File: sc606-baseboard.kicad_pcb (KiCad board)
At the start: 6 copper layers, 100 x 90 mm, 425 parts, among them IC1 TPS54561DPRT, IC2 TPS7A0518PDBVT, J1 PJ-202A, J10 WE_632723300011, J11 WE_632723300011, J12 U_FL-R-SMT-1_10_, J13 WE_632723300011, J14 CONMMCX002-SMD-T, J2 WE_68715014522, J3 F52R-1A7H1-11020, J4 46756-1001, J5 U_FL-R-SMT-1_10_, J6 U_FL-R-SMT-1_10_, J7 DM3AT-SF-PEJM5, J8 693022010811, J9 0473460001, M1 SC606T, Q1 BSS138APW, Q2 BSS138-7-F, Q3 BSS138APW, Q4 BSS138APW, Q5 BSS138APW, Q6 BSS138APW, Q7 BSS138-7-F, Q8 BSS138-7-F, SW1 1X03, U1 AP62301WU-7, U10 NCP163ASN330T1G, U11 EMIF06-MSD02N16, U12 FSUSB30MUX, U13 FT232RQ-REEL, U15 USB57442G, U2 AP62301WU-7, U3 AP62301WU-7, U4 74LVC1G123GN, U5 NTS0102GT, U6 PCA9547BS, U7 LT9611UXC, U8 NTS0102GT, U9 TPD13S523PWR, Y1 ABM8G-24.000MHZ-18-D2Y-T, Y2 ABM8G-25.000MHZ-B4Y-T

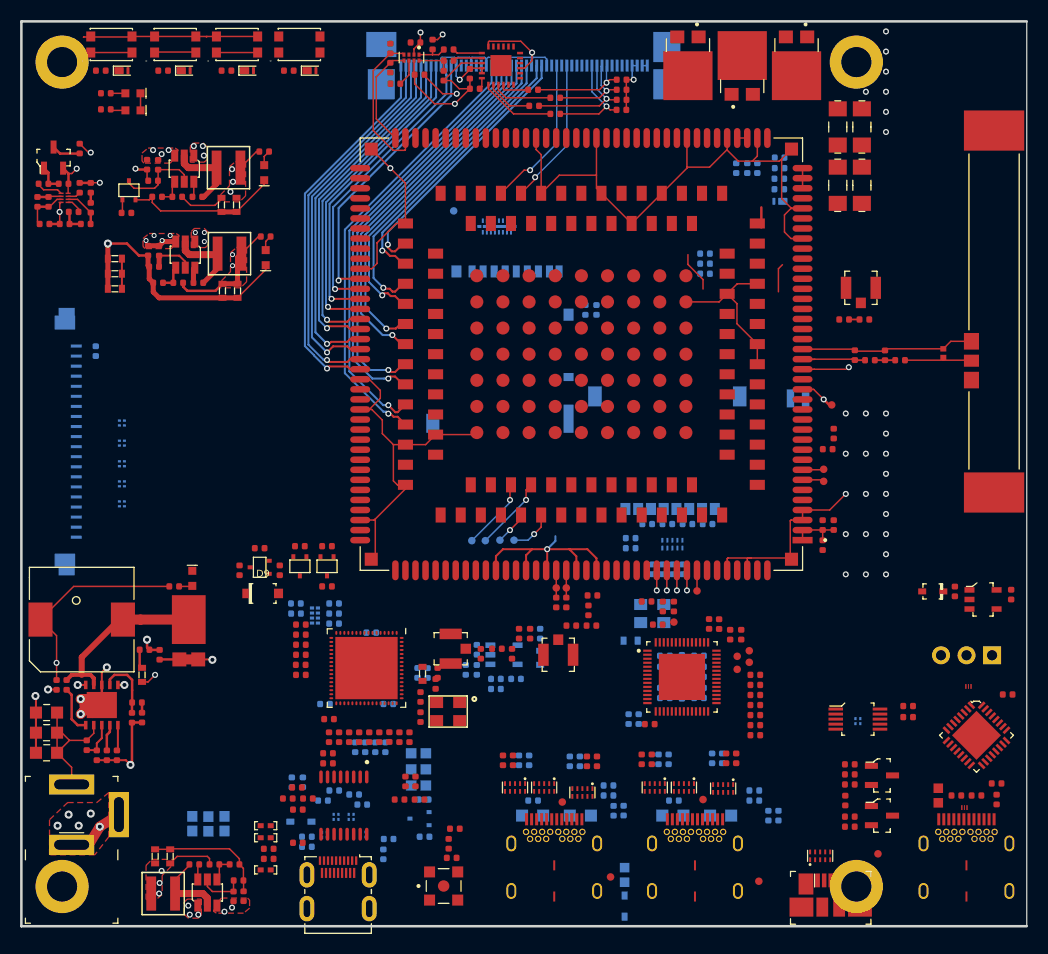
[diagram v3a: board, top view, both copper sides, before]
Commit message: USB Debug changed to micro USB. Started modifications on shortening board by 1cm
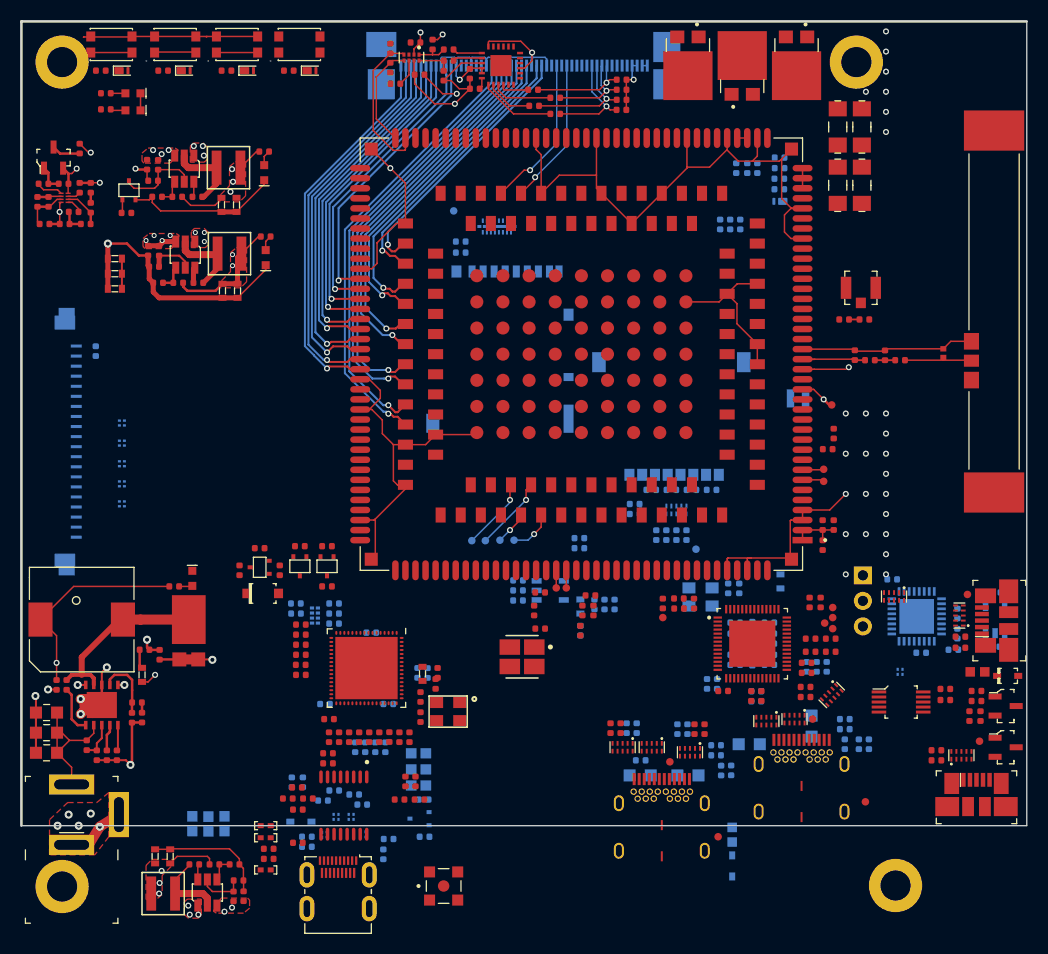
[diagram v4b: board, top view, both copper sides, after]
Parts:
- removed J10: WE_632723300011, sc606-baseboard-footprints:WE_632723300011
- removed J12: U_FL-R-SMT-1_10_, sc606-baseboard-footprints:Coax_Conn_U.FL
- removed R138, R139, R140: R_0R_0402, sc606-baseboard-footprints:0402-res
- added ANT1: 47948-0001, antmicro-footprints:47948-0001, F.Cu at (124.8, 103.2)
- added TP20: TP_SMD_0_75MM, sc606-baseboard-footprints:Testpoint_smd_0_75mm, F.Cu at (169.1, 97.1)
- C111, C112, C113, C114, C115, C116, C117, C118, C119, C126, C130, C132, IC2, R2, R3, TP2, U13: moved to B.Cu
- C142: value C_1u_0402 -> C_100n_0402
- C143: value C_1u_0402 -> C_4u7_0402
- D21, D23: value PESD5V0C2BDFZ -> PUSB3F96X_PASS; footprint sc606-baseboard-footprints:DFN0603-3 -> sc606-baseboard-footprints:PUSB3F96X
- J6: value U_FL-R-SMT-1_10_ -> 0473460001; footprint sc606-baseboard-footprints:Coax_Conn_U.FL -> sc606-baseboard-footprints:USB_Micro_B_Female_0473460001
- R134, R135: moved to F.Cu
- moved C143 54.7 mm to (168.4, 102.3), turned to 180 degrees
- moved C142 53.8 mm to (168.4, 101.2), turned to 180 degrees
- moved J6 44.9 mm to (173.2, 99.6), turned to 270 degrees
- moved D21 19.1 mm to (168.3, 99.1), turned to 90 degrees
- moved C112 18.1 mm to (168.1, 98.9), turned to 90 degrees
- moved C151 17.9 mm to (156.9, 111.9), turned to 90 degrees
- moved J9 17.6 mm to (170.0, 118.1)
- moved D20 17.2 mm to (168.5, 113.0)
- moved C113 16.2 mm to (161.6, 95.5), turned to 180 degrees
- moved C114 16.2 mm to (168.1, 100.9), turned to 270 degrees
- moved R113 16.0 mm to (150.5, 95.7), turned to 270 degrees
- moved C117 15.5 mm to (167.7, 102.5), turned to 180 degrees
- moved SW1 15.1 mm to (158.7, 95.1), turned to 0 degrees
- moved TP12 15.1 mm to (170.3, 111.7)
- moved C116 15.0 mm to (164.5, 102.8)
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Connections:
- C142 pad 1: Net-(C142-Pad1) -> /USB_flash_debug/DBG_VBUS
- C143 pad 1: Net-(C143-Pad1) -> /USB_flash_debug/DBG_VBUS
- C89 pad 1: Net-(C89-Pad1) -> ANT-WIFI
- D23 pad 1: DEBUG_UART_RX -> Net-(D23-Pad1)
- D23 pad 2: DEBUG_UART_TX -> Net-(D23-Pad2)
- D32 pad 1: /USB_HUB_Connectors/USB_C2_SS_C_TX2_N -> /USB_HUB_Connectors/USB_C2_SS_C_RX2_P
- D32 pad 10: /USB_HUB_Connectors/USB_C2_SS_C_TX2_N -> /USB_HUB_Connectors/USB_C2_SS_C_RX2_P
- D32 pad 2: /USB_HUB_Connectors/USB_C2_SS_C_TX2_P -> /USB_HUB_Connectors/USB_C2_SS_C_RX2_N
- D32 pad 4: /USB_HUB_Connectors/USB_C2_SS_C_RX2_P -> /USB_HUB_Connectors/USB_C2_SS_C_TX2_N
- D32 pad 5: /USB_HUB_Connectors/USB_C2_SS_C_RX2_N -> /USB_HUB_Connectors/USB_C2_SS_C_TX2_P
- D32 pad 6: /USB_HUB_Connectors/USB_C2_SS_C_RX2_N -> /USB_HUB_Connectors/USB_C2_SS_C_TX2_P
- D32 pad 7: /USB_HUB_Connectors/USB_C2_SS_C_RX2_P -> /USB_HUB_Connectors/USB_C2_SS_C_TX2_N
- D32 pad 9: /USB_HUB_Connectors/USB_C2_SS_C_TX2_P -> /USB_HUB_Connectors/USB_C2_SS_C_RX2_N
- J14 pad 1: Net-(C143-Pad1) -> Net-(C101-Pad1)
- J6 pad 1: GND -> /USB_flash_debug/DBG_VBUS
- J6 pad 2: Net-(C101-Pad1) -> /USB_flash_debug/DBG_USB_D_N
- R126 pad 1: Net-(C89-Pad1) -> ANT-WIFI
- SW1 pad 1: DEBUG_UART_RX -> DEBUG_UART_TX
- SW1 pad 2: DEBUG_UART_TX -> DEBUG_UART_RX
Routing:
- net GND: track 350.0 -> 328.2 mm, vias 56 -> 54
- net SD_DATA_6: track 4.05 -> 0.00 mm
- net SD_LDO11: track 2.87 -> 0.00 mm
- net (no net): track 2.40 -> 0.00 mm
- net USIM1_VDD: track 2.14 -> 0.00 mm, vias 1 -> 0
- net Net-(M1-Pad145): track 2.05 -> 0.00 mm
- net USIM1_RST: track 2.00 -> 0.00 mm, vias 1 -> 0
- net USIM1_DATA: track 2.00 -> 0.00 mm, vias 1 -> 0
- net USIM1_CLK: track 2.00 -> 0.00 mm, vias 1 -> 0
- net Net-(M1-Pad132): track 2.72 -> 1.75 mm
- net Net-(M1-Pad131): track 2.72 -> 1.75 mm
- net DEBUG_UART_TX: vias 0 -> 1
- added copper zone on In1.Power_Plane, net GND
- removed copper zone on In1.GND, net GND
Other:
- board size 100 x 90 mm -> 100 x 80 mm
- net class CSI_DSI_Inner removed
- net class CSI_DSI_Outer removed
- net class Default: clearance 0.15 -> 0.125; trace_width 0.15 -> 0.125
- net class HDMI_Inner removed
- net class SE50_inner added: clearance 0.125, trace_width 0.162, via_dia 0.6, via_drill 0.35
- net class SE50_outer added: clearance 0.125, trace_width 0.182, via_dia 0.6, via_drill 0.35
- net class Z100_inner added: clearance 0.125, trace_width 0.162, via_dia 0.6, via_drill 0.35
- net class Z100_outer added: clearance 0.125, trace_width 0.182, via_dia 0.6, via_drill 0.35
- net class Z90_inner added: clearance 0.125, trace_width 0.193, via_dia 0.6, via_drill 0.35
- net class Z90_outer added: clearance 0.125, trace_width 0.215, via_dia 0.6, via_drill 0.35
- rule trace_clearance: 0.15 -> 0.125
- rule trace_min: 0.15 -> 0.125

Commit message: Finished placement after shortening board by 1cm
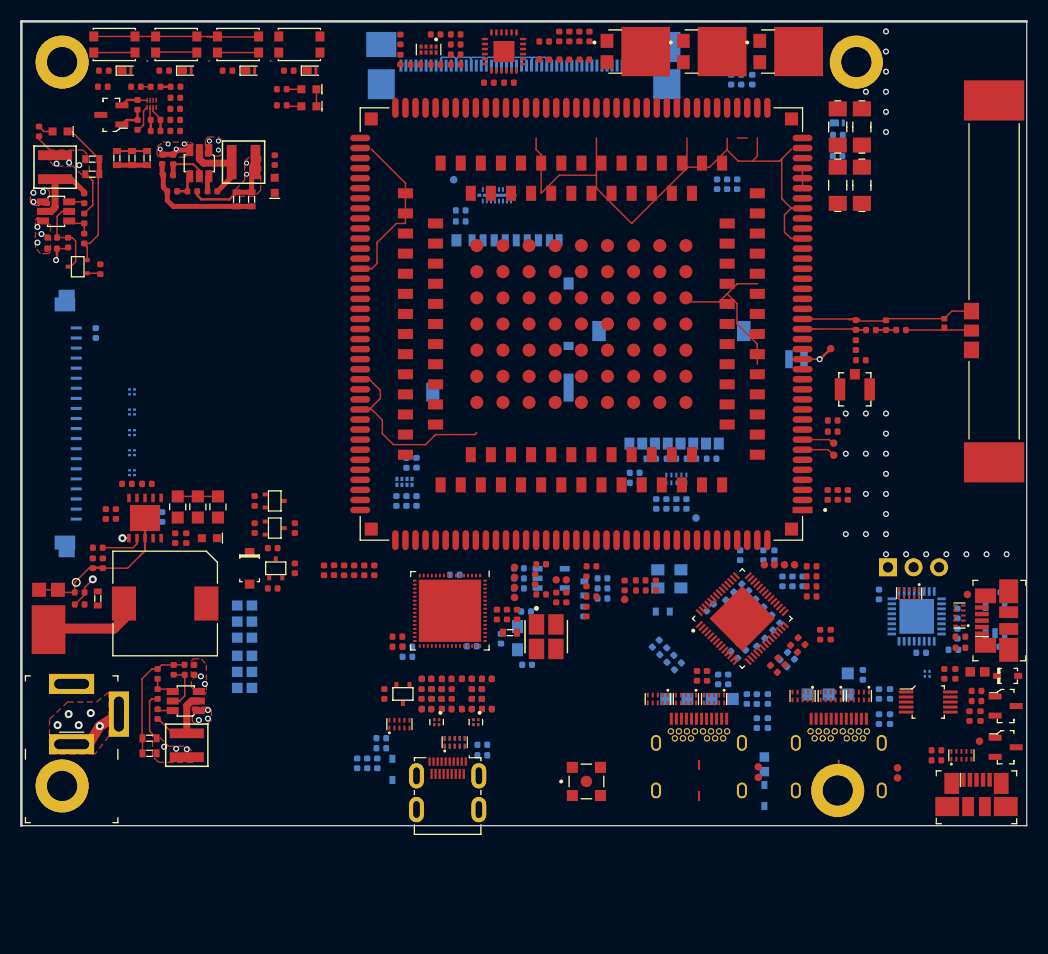
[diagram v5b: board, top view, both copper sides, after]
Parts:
- removed C83, C84: C_100n_0402, sc606-baseboard-footprints:0402-cap
- removed D7, D8: TPD1E10B06DPYR, sc606-baseboard-footprints:XDFN-2_1x0.60mm
- removed R155, R156, R157, R158: R_0R_0402, sc606-baseboard-footprints:0402-res
- removed U9: TPD13S523PWR, sc606-baseboard-footprints:TSSOP-16
- added D29: PUSB3F96X_PASS, sc606-baseboard-footprints:PUSB3F96X, F.Cu at (118.1, 111.7)
- added D30: PUSB3F96X_PASS, sc606-baseboard-footprints:PUSB3F96X, B.Cu at (118.1, 111.7)
- added R138: R_56k_0402, antmicro-footprints:0402-res, B.Cu at (161.4, 106.9)
- added R139: R_56k_0402, antmicro-footprints:0402-res, B.Cu at (161.4, 109.4)
- added R140: R_56k_0402, antmicro-footprints:0402-res, B.Cu at (160.3, 106.9)
- added R141: R_56k_0402, antmicro-footprints:0402-res, B.Cu at (160.3, 109.4)
- C128, C25, C53, C57, R118, R119, R130, R133, R136, R137, R52, R61, R62, R65, R66, R67, R68, R88, Y1: moved to B.Cu
- C147, C149, C67, C68, C77, C78, C80, L16, L18, Q3, R2, R3, TP5, TP6, TP7, TP8: moved to F.Cu
- D6: value TPD1E10B06DPYR -> PUSB3F96X_PASS; footprint sc606-baseboard-footprints:XDFN-2_1x0.60mm -> sc606-baseboard-footprints:PUSB3F96X
- R123, R125, R131, R132: value R_0R_0402 -> R_56k_0402; footprint sc606-baseboard-footprints:0402-res -> antmicro-footprints:0402-res
- moved C19 29.8 mm to (94.5, 88.3), turned to 270 degrees
- moved R5 27.2 mm to (85.5, 86.0), turned to 180 degrees
- moved C17 27.0 mm to (92.5, 88.3), turned to 270 degrees
- moved R4 26.7 mm to (87.5, 86.0), turned to 180 degrees
- moved C18 24.3 mm to (90.5, 88.3), turned to 270 degrees
- moved C20 24.0 mm to (83.4, 89.0)
- moved R6 24.0 mm to (84.4, 89.0)
- moved C21 23.6 mm to (91.7, 104.0), turned to 180 degrees
- moved L5 22.7 mm to (97.2, 98.1)
- moved L6 22.7 mm to (97.2, 99.7)
- moved L7 22.7 mm to (97.2, 101.3)
- moved R106 22.5 mm to (76.8, 51.0), turned to 90 degrees
- moved R7 22.5 mm to (91.7, 105.0), turned to 180 degrees
- moved R8 21.9 mm to (90.2, 104.5), turned to 90 degrees
- moved D19 20.7 mm to (78.8, 51.0), turned to 180 degrees
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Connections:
- D10 pad A: Net-(C84-Pad1) -> 5V0_SYS
- D25 pad 1: /USB_HUB_Connectors/USB_C1_D1_N -> /USB_HUB_Connectors/USB_C1_D2_N
- D25 pad 10: /USB_HUB_Connectors/USB_C1_D1_N -> /USB_HUB_Connectors/USB_C1_D2_N
- D25 pad 2: /USB_HUB_Connectors/USB_C1_D1_P -> /USB_HUB_Connectors/USB_C1_D2_P
- D25 pad 4: /USB_HUB_Connectors/USB_C1_D2_N -> /USB_HUB_Connectors/USB_C1_D1_N
- D25 pad 5: /USB_HUB_Connectors/USB_C1_D2_P -> /USB_HUB_Connectors/USB_C1_D1_P
- D25 pad 6: /USB_HUB_Connectors/USB_C1_D2_P -> /USB_HUB_Connectors/USB_C1_D1_P
- D25 pad 7: /USB_HUB_Connectors/USB_C1_D2_N -> /USB_HUB_Connectors/USB_C1_D1_N
- D25 pad 9: /USB_HUB_Connectors/USB_C1_D1_P -> /USB_HUB_Connectors/USB_C1_D2_P
- D26 pad 1: /USB_HUB_Connectors/USB_C2_SS_C_TX1_N -> /USB_HUB_Connectors/USB_C2_SS_C_RX1_N
- D26 pad 10: /USB_HUB_Connectors/USB_C2_SS_C_TX1_N -> /USB_HUB_Connectors/USB_C2_SS_C_RX1_N
- D26 pad 2: /USB_HUB_Connectors/USB_C2_SS_C_TX1_P -> /USB_HUB_Connectors/USB_C2_SS_C_RX1_P
- D26 pad 4: /USB_HUB_Connectors/USB_C2_SS_C_RX1_N -> /USB_HUB_Connectors/USB_C2_SS_C_TX1_N
- D26 pad 5: /USB_HUB_Connectors/USB_C2_SS_C_RX1_P -> /USB_HUB_Connectors/USB_C2_SS_C_TX1_P
- D26 pad 6: /USB_HUB_Connectors/USB_C2_SS_C_RX1_P -> /USB_HUB_Connectors/USB_C2_SS_C_TX1_P
- D26 pad 7: /USB_HUB_Connectors/USB_C2_SS_C_RX1_N -> /USB_HUB_Connectors/USB_C2_SS_C_TX1_N
- D26 pad 9: /USB_HUB_Connectors/USB_C2_SS_C_TX1_P -> /USB_HUB_Connectors/USB_C2_SS_C_RX1_P
- D27 pad 1: /USB_HUB_Connectors/USB_C1_SS_C_TX2_N -> /USB_HUB_Connectors/USB_C1_SS_C_RX2_P
- D27 pad 10: /USB_HUB_Connectors/USB_C1_SS_C_TX2_N -> /USB_HUB_Connectors/USB_C1_SS_C_RX2_P
- D27 pad 2: /USB_HUB_Connectors/USB_C1_SS_C_TX2_P -> /USB_HUB_Connectors/USB_C1_SS_C_RX2_N
- D27 pad 4: /USB_HUB_Connectors/USB_C1_SS_C_RX2_P -> /USB_HUB_Connectors/USB_C1_SS_C_TX2_N
- D27 pad 5: /USB_HUB_Connectors/USB_C1_SS_C_RX2_N -> /USB_HUB_Connectors/USB_C1_SS_C_TX2_P
- D27 pad 6: /USB_HUB_Connectors/USB_C1_SS_C_RX2_N -> /USB_HUB_Connectors/USB_C1_SS_C_TX2_P
- D27 pad 7: /USB_HUB_Connectors/USB_C1_SS_C_RX2_P -> /USB_HUB_Connectors/USB_C1_SS_C_TX2_N
- D27 pad 9: /USB_HUB_Connectors/USB_C1_SS_C_TX2_P -> /USB_HUB_Connectors/USB_C1_SS_C_RX2_N
- D28 pad 1: /USB_HUB_Connectors/USB_C1_SS_C_TX1_N -> /USB_HUB_Connectors/USB_C1_SS_C_RX1_N
- D28 pad 10: /USB_HUB_Connectors/USB_C1_SS_C_TX1_N -> /USB_HUB_Connectors/USB_C1_SS_C_RX1_N
- D28 pad 2: /USB_HUB_Connectors/USB_C1_SS_C_TX1_P -> /USB_HUB_Connectors/USB_C1_SS_C_RX1_P
- D28 pad 4: /USB_HUB_Connectors/USB_C1_SS_C_RX1_N -> /USB_HUB_Connectors/USB_C1_SS_C_TX1_N
- D28 pad 5: /USB_HUB_Connectors/USB_C1_SS_C_RX1_P -> /USB_HUB_Connectors/USB_C1_SS_C_TX1_P
- D28 pad 6: /USB_HUB_Connectors/USB_C1_SS_C_RX1_P -> /USB_HUB_Connectors/USB_C1_SS_C_TX1_P
- D28 pad 7: /USB_HUB_Connectors/USB_C1_SS_C_RX1_N -> /USB_HUB_Connectors/USB_C1_SS_C_TX1_N
- D28 pad 9: /USB_HUB_Connectors/USB_C1_SS_C_TX1_P -> /USB_HUB_Connectors/USB_C1_SS_C_RX1_P
- D31 pad 1: /USB_HUB_Connectors/USB_C2_D1_N -> /USB_HUB_Connectors/USB_C2_D2_P
- D31 pad 10: /USB_HUB_Connectors/USB_C2_D1_N -> /USB_HUB_Connectors/USB_C2_D2_P
- D31 pad 2: /USB_HUB_Connectors/USB_C2_D1_P -> /USB_HUB_Connectors/USB_C2_D2_N
- D31 pad 4: /USB_HUB_Connectors/USB_C2_D2_N -> /USB_HUB_Connectors/USB_C2_D1_N
- D31 pad 5: /USB_HUB_Connectors/USB_C2_D2_P -> /USB_HUB_Connectors/USB_C2_D1_P
- D31 pad 6: /USB_HUB_Connectors/USB_C2_D2_P -> /USB_HUB_Connectors/USB_C2_D1_P
- D31 pad 7: /USB_HUB_Connectors/USB_C2_D2_N -> /USB_HUB_Connectors/USB_C2_D1_N
- D31 pad 9: /USB_HUB_Connectors/USB_C2_D1_P -> /USB_HUB_Connectors/USB_C2_D2_N
- D6 pad 1: GND -> Net-(D6-Pad1)
- D6 pad 2: /display module/LTtoHDMI_SCL -> /display module/LTtoHDMI_SDA
- J11 pad A5: Net-(J11-PadA5) -> /USB_HUB_Connectors/USB_C1_CC1
- J11 pad B5: Net-(J11-PadB5) -> /USB_HUB_Connectors/USB_C1_CC2
- J13 pad A5: Net-(J13-PadA5) -> /USB_HUB_Connectors/USB_C2_CC1
- J13 pad B5: Net-(J13-PadB5) -> /USB_HUB_Connectors/USB_C2_CC2
- L16 pad 1: /display module/TX_D2_C_N -> /display module/TX_D2_C_P
- L16 pad 2: /display module/TX_D2_Ferr_N -> /display module/TX_D2_Ferr_P
- L16 pad 3: /display module/TX_D2_Ferr_P -> /display module/TX_D2_Ferr_N
- L16 pad 4: /display module/TX_D2_C_P -> /display module/TX_D2_C_N
- L18 pad 1: /display module/TX_D0_C_N -> /display module/TX_D0_C_P
- L18 pad 2: /display module/TX_D0_Ferr_N -> /display module/TX_D0_Ferr_P
- L18 pad 3: /display module/TX_D0_Ferr_P -> /display module/TX_D0_Ferr_N
- L18 pad 4: /display module/TX_D0_C_P -> /display module/TX_D0_C_N
- R123 pad 1: /USB_HUB_Connectors/USB_C1_CC2 -> /USB_HUB_Connectors/5V0_USB
- R123 pad 2: Net-(J11-PadA5) -> /USB_HUB_Connectors/USB_C1_CC1
- R125 pad 2: Net-(J11-PadA5) -> GND
- R131 pad 1: /USB_HUB_Connectors/USB_C1_CC1 -> /USB_HUB_Connectors/5V0_USB
- R131 pad 2: Net-(J11-PadB5) -> /USB_HUB_Connectors/USB_C1_CC2
- R132 pad 2: Net-(J11-PadB5) -> GND
- R61 pad 2: /display module/LTtoHDMI_SCL -> /display module/LTtoHDMI_SDA
- R62 pad 2: /display module/LTtoHDMI_SDA -> /display module/LTtoHDMI_SCL
- SW1 pad 1: DEBUG_UART_TX -> DEBUG_UART_RX
- SW1 pad 2: DEBUG_UART_RX -> DEBUG_UART_TX
- U15 pad 29: /USB_HUB_Connectors/USB_C2_SS_RX2_N -> /USB_HUB_Connectors/USB_C2_SS_RX2_P
- U15 pad 30: /USB_HUB_Connectors/USB_C2_SS_RX2_P -> /USB_HUB_Connectors/USB_C2_SS_RX2_N
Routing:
- net GND: track 328.2 -> 239.3 mm, vias 54 -> 37
- net CAM2_D3_N: track 44.8 -> 0.00 mm, vias 1 -> 0
- net CAM2_D3_P: track 44.0 -> 0.00 mm, vias 1 -> 0
- net 5V0_SYS: track 50.7 -> 7.70 mm, vias 13 -> 9
- net CAM2_D2_N: track 41.7 -> 0.00 mm, vias 1 -> 0
- net CAM2_D2_P: track 40.9 -> 0.00 mm, vias 1 -> 0
- net CAM1_D3_N: track 38.5 -> 0.00 mm, vias 1 -> 0
- net CAM1_D3_P: track 37.7 -> 0.00 mm, vias 1 -> 0
- net CAM1_D2_N: track 36.9 -> 0.00 mm, vias 1 -> 0
- net CAM2_D1_N: track 36.5 -> 0.00 mm, vias 1 -> 0
- net CAM1_D2_P: track 35.8 -> 0.00 mm, vias 1 -> 0
- net CAM2_D1_P: track 35.3 -> 0.00 mm, vias 1 -> 0
- net CAM1_D1_N: track 34.2 -> 0.00 mm, vias 1 -> 0
- net 3V3_SYS: track 43.2 -> 9.42 mm, vias 4 -> 2
- net CAM1_D1_P: track 33.2 -> 0.00 mm, vias 1 -> 0
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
